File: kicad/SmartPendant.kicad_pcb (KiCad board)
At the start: 2 copper layers, 130.9 x 55 mm, 50 parts, among them J1 UART, J2 ST-LINK, J3 Conn_01x05, J4 TYPE-C16PIN, J5 Display, Q1 MMBT3904, U1 WEACT BLACKPILL F4X1, U2 AMS1117-3.3, U3 MB85RC256VPNF

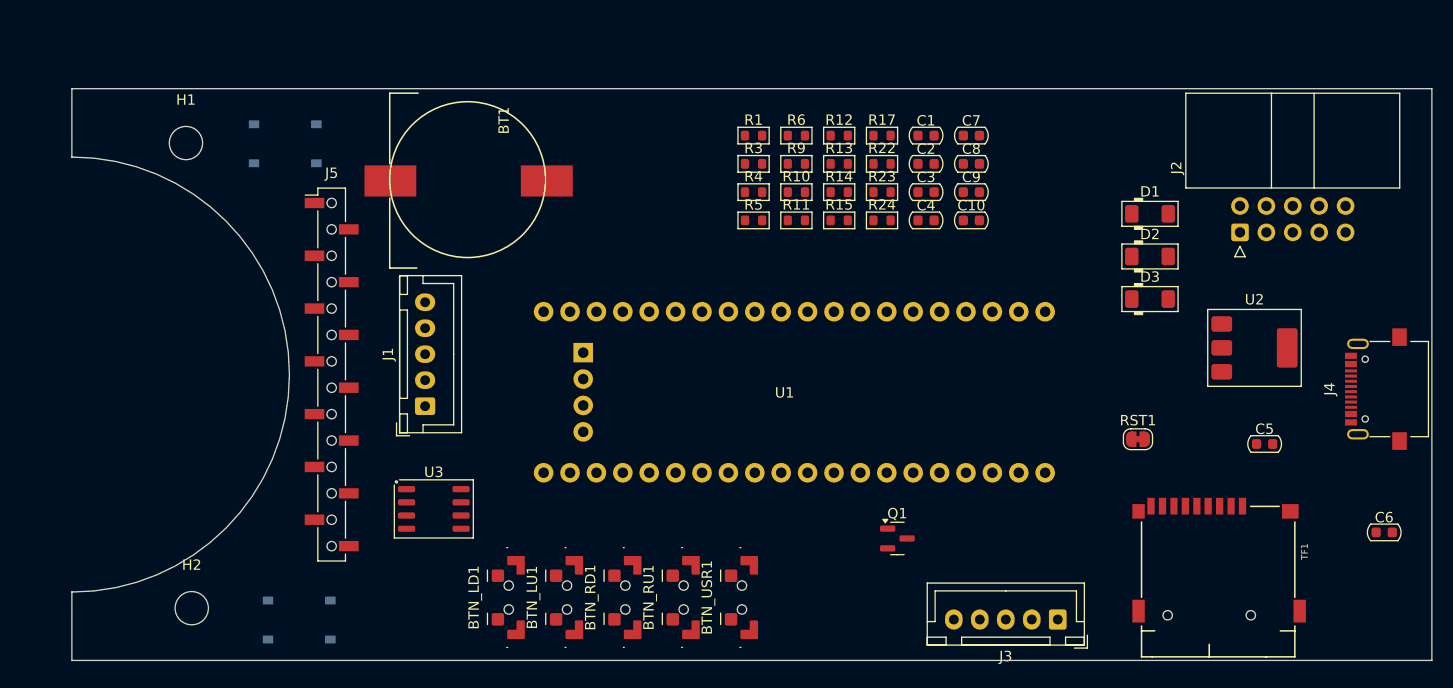
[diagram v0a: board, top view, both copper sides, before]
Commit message: Fix some component positions.
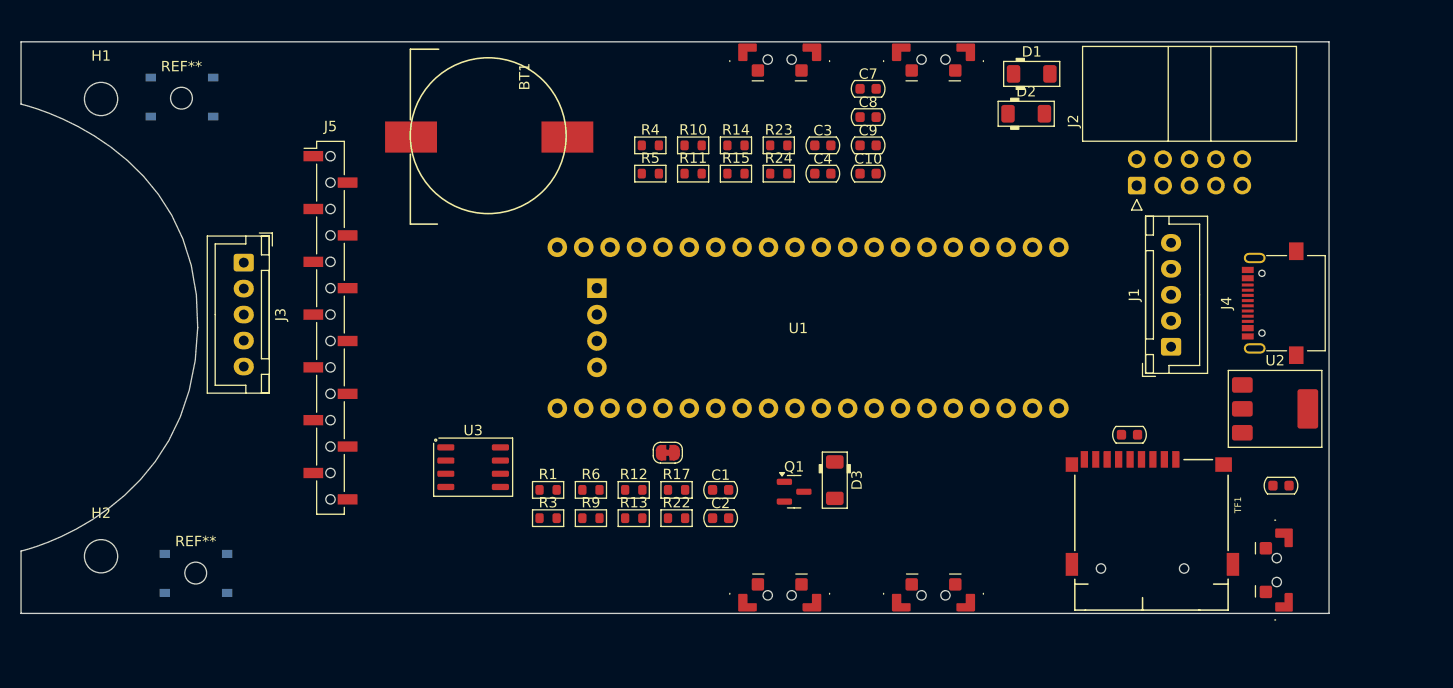
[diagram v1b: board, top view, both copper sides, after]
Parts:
- added REF**: MountingHole_2.1mm, MountingHole:MountingHole_2.1mm, F.Cu at (141.8, 101.1)
- added REF**: MountingHole_2.1mm, MountingHole:MountingHole_2.1mm, F.Cu at (140.4, 55.4)
- moved J3 85.5 mm to (146.4, 71.2), turned to -90 degrees
- moved J1 72.0 mm to (235.7, 79.3)
- moved BTN_LU1 62.4 mm to (212.8, 52.5), turned to 180 degrees
- moved BTN_LD1 57.6 mm to (198.0, 52.5), turned to 180 degrees
- moved BTN_USR1 51.5 mm to (245.1, 100.8)
- moved RST1 45.3 mm to (187.2, 89.5)
- moved C1 39.4 mm to (192.3, 93.1)
- moved C2 39.4 mm to (192.3, 95.8)
- moved R1 39.4 mm to (175.7, 93.1)
- moved R12 39.4 mm to (184.0, 93.1)
- moved R13 39.4 mm to (184.0, 95.8)
- moved R3 39.4 mm to (175.7, 95.8)
- moved R6 39.4 mm to (179.8, 93.1)
- moved R9 39.4 mm to (179.8, 95.8)
- moved R17 39.4 mm to (188.1, 93.1)
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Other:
- board size 130.9 x 55 mm -> 125.9 x 55 mm

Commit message: Move components around.
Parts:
- removed REF** (x2): MountingHole_2.1mm, MountingHole:MountingHole_2.1mm
- BTN_LD1, BTN_LU1, BTN_RD1, BTN_RU1, BTN_USR1: footprint SmartPendant:SMD_Push_Side_button_3x6x3.5mm -> Custom:SMD_Push_Side_button_3x6x3.5mm
- moved R3 67.2 mm to (240.1, 76.4), turned to 180 degrees
- moved R13 58.9 mm to (242.4, 103.3), turned to -90 degrees
- moved R4 56.2 mm to (240.1, 73.4), turned to 180 degrees
- moved R9 54.0 mm to (215.6, 55.3)
- moved R22 50.7 mm to (238.1, 87.3), turned to -90 degrees
- moved R15 47.9 mm to (237.7, 81.9), turned to 90 degrees
- moved R10 46.6 mm to (214.2, 99.6)
- moved R23 46.1 mm to (235.1, 87.3), turned to -90 degrees
- moved R24 39.2 mm to (228.4, 87.3), turned to -90 degrees
- moved R5 38.9 mm to (147.5, 54.3), turned to 90 degrees
- moved R14 38.3 mm to (159.0, 76.0), turned to -90 degrees
- moved R17 35.4 mm to (223.3, 89.2)
- moved R6 33.2 mm to (147.4, 100.0), turned to 90 degrees
- moved R1 23.4 mm to (198.8, 89.5)
- moved R12 14.4 mm to (196.7, 99.8), turned to 180 degrees
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
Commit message: Fix ERC violations.
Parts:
- removed J4: TYPE-C16PIN, Custom:USB_C_Receptacle_AliExpress_16pin
- removed TF1: TF-115, Custom:J_SD_Card-micro_socket_A
- added J6: USB_C_Receptacle_USB2.0_16P, Custom:USB_C_Receptacle_AliExpress_16pin, F.Cu at (246.6, 75.1)
- added J8: Micro_SD_Card_Det1, Custom:J_SD_Card-micro_socket_A, F.Cu at (231.4, 97.5)
- D1, D2: value 1N5819WS -> 1N5819; footprint PCM_Diode_SMD_AKL:D_MiniMELF -> PCM_Diode_SMD_AKL:D_SOD-123
- R17: value 1kΩ -> 1k
- R22, R23, R24: value 10kΩ -> 10k
- R3, R4: value 5.1kΩ -> 5k1
- U3: value MB85RC256VPNF -> MB85RC256VPNF-G-JNERE1
- moved D2 2.76 mm to (222.3, 59.6)
- moved R13 1.23 mm to (242.3, 102.1)
- moved R23 0.58 mm to (234.5, 87.3)
- moved R11 0.45 mm to (196.5, 55.4)
- moved BTN_LD1 0.44 mm to (198.0, 52.9)
- moved BTN_LU1 0.44 mm to (212.8, 52.9)
- moved BTN_USR1 0.43 mm to (245.1, 100.4)
- moved BTN_RD1 0.41 mm to (198.0, 102.1)
- moved BTN_RU1 0.41 mm to (212.8, 102.1)

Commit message: Use angle JST connectors.
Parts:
- J1: footprint Connector_JST:JST_XH_B5B-XH-A_1x05_P2.50mm_Vertical -> Custom:JST_XH_S5B-XH-A_1x05_P2.50mm_Horizontal_Compact
- J3: value Conn_01x05 -> Encoder; footprint Connector_JST:JST_XH_B5B-XH-A_1x05_P2.50mm_Vertical -> Custom:JST_XH_S5B-XH-A_1x05_P2.50mm_Horizontal_Compact
- moved J1 6.38 mm to (224.9, 81.7)
- moved J3 3.62 mm to (150.0, 71.6)

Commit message: Optimize component placement.
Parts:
- moved C8 56.4 mm to (150.4, 62.5), turned to -90 degrees
- moved D1 31.1 mm to (239.0, 79.3)
- moved C10 29.7 mm to (177.0, 65.7), turned to 180 degrees
- moved D2 19.8 mm to (240.7, 66.9), turned to 180 degrees
- moved J3 19.2 mm to (149.9, 90.8)
- moved C9 19.2 mm to (222.3, 70.9), turned to -90 degrees
- moved R6 7.60 mm to (154.8, 101.5)
- moved R15 3.14 mm to (234.7, 82.9)

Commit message: Tweak layout.
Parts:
- moved J8 39.9 mm to (231.4, 57.6), turned to 0 degrees
- moved J2 27.7 mm to (237.2, 91.2), turned to -90 degrees
- moved U2 25.3 mm to (245.1, 60.0)
- moved R13 7.67 mm to (245.6, 95.1), turned to 0 degrees
- moved BTN_L1 7.52 mm to (148.0, 55.0)
- moved R6 6.79 mm to (148.1, 100.8)
- moved BTN_R1 6.27 mm to (148.0, 100.0)
- moved J3 5.60 mm to (150.2, 85.2)
- moved J6 4.87 mm to (246.6, 80.0)
- moved R15 3.66 mm to (238.4, 82.9)
- moved R10 2.52 mm to (216.7, 99.5)
- moved R17 1.33 mm to (223.7, 87.9)
- moved BTN_LU1 1.30 mm to (214.1, 52.9)
- moved BTN_RU1 1.30 mm to (214.1, 102.1)
- moved J5 1.22 mm to (156.0, 77.5)
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
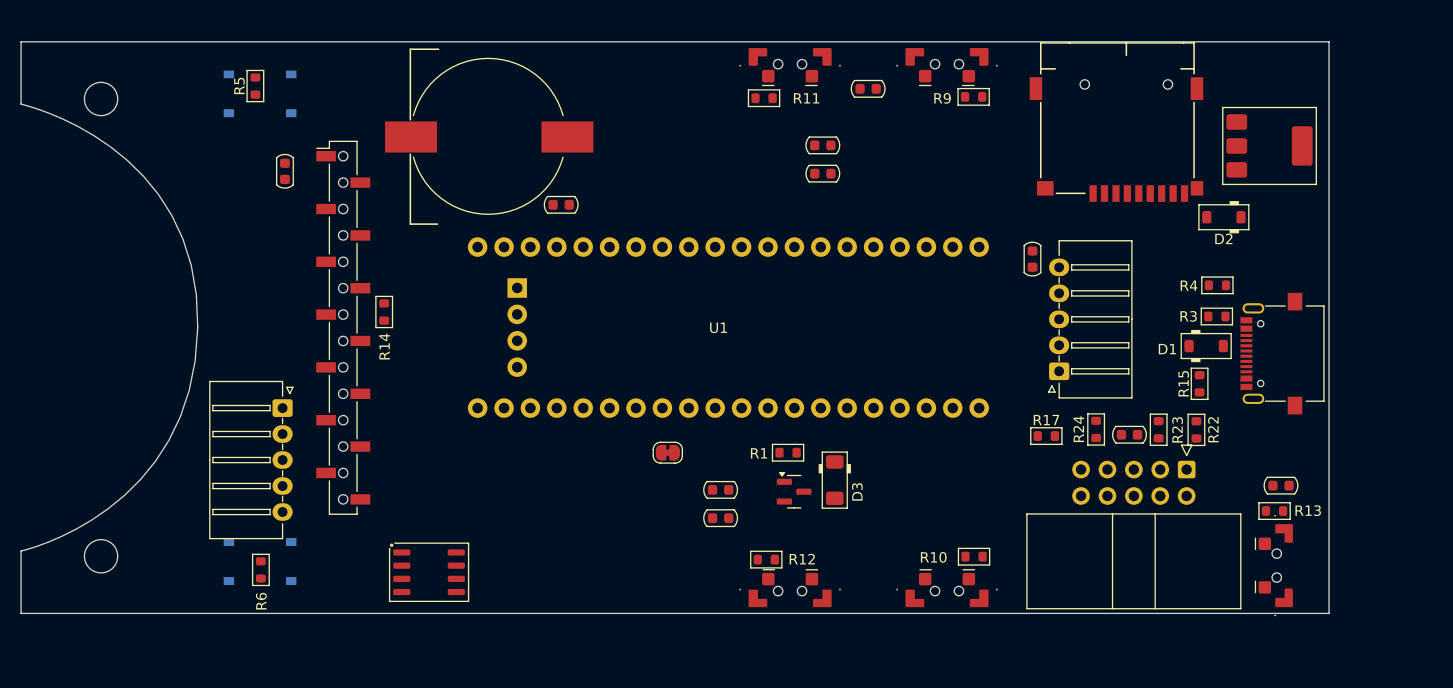
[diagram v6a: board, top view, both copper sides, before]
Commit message: Fix some footprint issues.
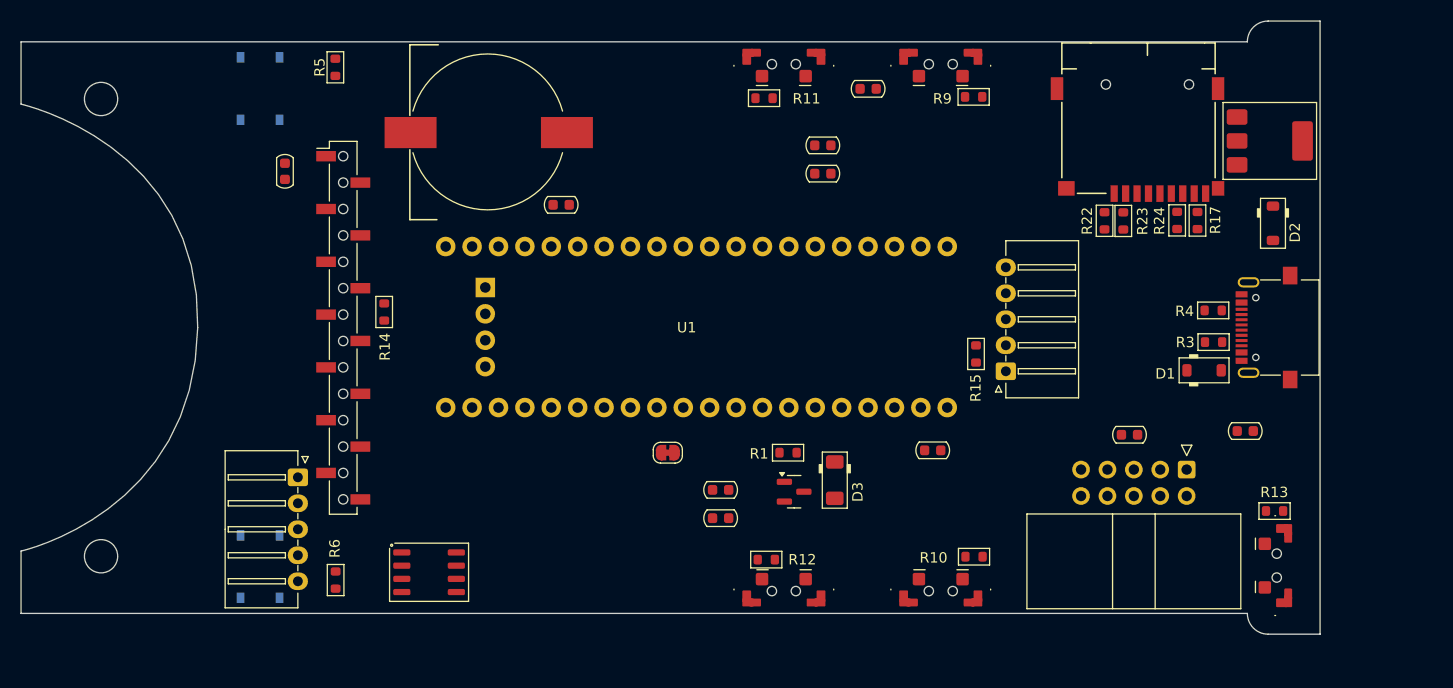
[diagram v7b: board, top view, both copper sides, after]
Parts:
- moved R17 25.3 mm to (238.2, 67.2), turned to 90 degrees
- moved R22 22.0 mm to (229.3, 67.2), turned to 90 degrees
- moved R15 21.7 mm to (216.9, 80.0), turned to -90 degrees
- moved R24 21.6 mm to (236.2, 67.2), turned to 90 degrees
- moved C9 20.8 mm to (212.7, 89.3), turned to 180 degrees
- moved R23 20.4 mm to (231.1, 67.2)
- moved R5 7.90 mm to (155.2, 52.5)
- moved R6 7.25 mm to (155.3, 101.8), turned to -90 degrees
- moved J3 6.82 mm to (151.6, 91.9)
- moved C6 6.28 mm to (242.8, 87.5)
- moved J1 5.13 mm to (219.8, 81.7)
- moved D2 4.76 mm to (245.5, 67.5), turned to -90 degrees
- moved U1 3.07 mm to (189.0, 77.4)
- moved J6 2.55 mm to (246.1, 77.5)
- moved R3 2.48 mm to (239.8, 78.9)
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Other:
- board size 125.9 x 55 mm -> 125 x 59 mm
